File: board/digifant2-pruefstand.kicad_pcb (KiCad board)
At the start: 2 copper layers, 144 x 169 mm, 76 parts, among them J0 VW ECU HARNESS, J1 12V BENCH IN, J2 IDLE VALVE N71, J3 OLED / UI I2C, Q1 2N7002, Q2 P-MOS -30V >=5A, Q3 2N7002, Q5 2N7002, SW1 PUSH, SW2 PUSH, SW3 PUSH, U1 INA226 (0x40), U2 MCP4728 (0x60), U3 INA226 (0x41), U4 AD9833, U5 Raspberry Pi Pico, U6 TS5A3159A, U7 TS5A3159A, U8 TS5A3159A, Y1 25MHz

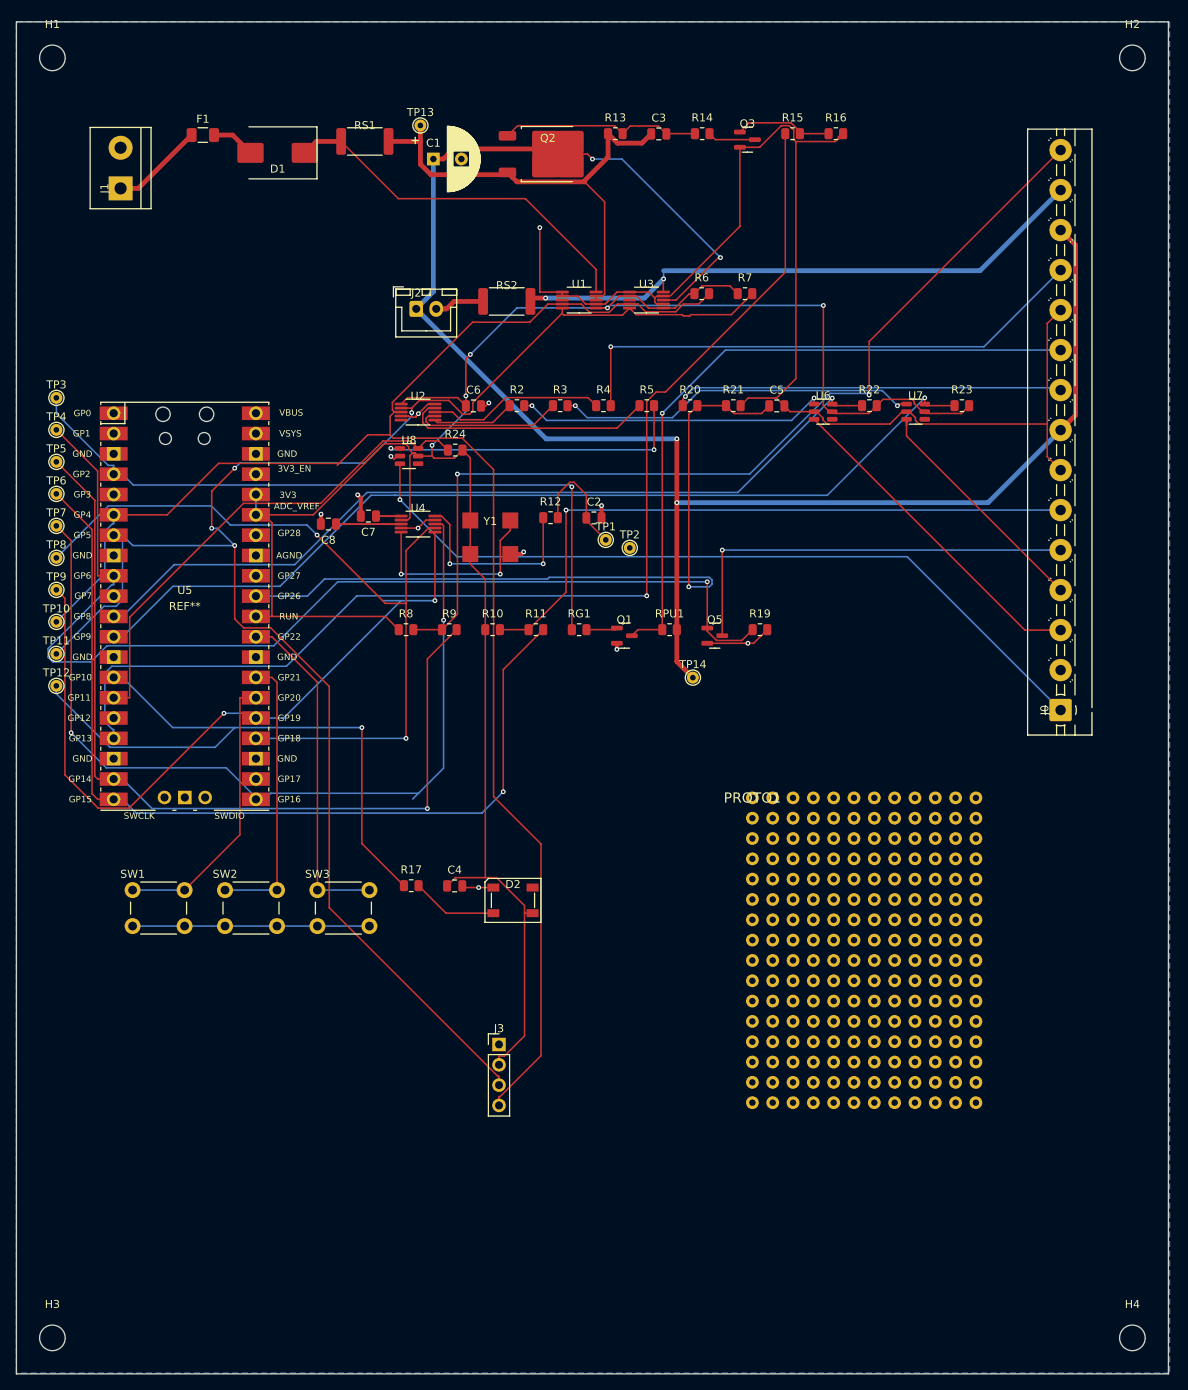
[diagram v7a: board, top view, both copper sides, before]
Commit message: Route remaining test points, add decoupling/thermal copper, trim board, label silkscreen
- Route TP7/TP8/TP9 (the three hardest, on U5's east side) with a purpose-built
  grid pathfinder after manual/Freerouting attempts kept snagging on the Pico's
  pin column, which has no usable gap anywhere along its length for a second
  trace; both had to detour around the south end of the module.
- Add C9/C10 (100nF) decoupling for U1/U3's VS pins per the INA226 datasheet,
  tapping the existing +3V3 trunk and GND pour near the packed U1/U3/RS1/RS2
  pocket.
- Add thermal copper pours for D1 (real risk: ~1.25W at sustained ~2.5A with
  no relief) and Q2, verified electrically connected via KiCad's connectivity
  API rather than just visually overlapping.
- Trim the board from 144x169mm to 144x150mm - the bottom 19mm was completely
  empty; move H3/H4 to keep the same edge margin as H1/H2.
- Add functional silkscreen labels next to J0 (real VW harness pin numbers)
  and every test point (moved from F.Fab, a documentation-only layer that
  never gets printed, to real F.SilkS; shortened long labels to fit the
  west-margin corridor without running off the board edge).
- Add fab-identification text (title/rev/date/company) to the previously
  empty back silkscreen, driven by the board's title block variables.
- Fix all 14 test points having "Exclude from BOM" set on the PCB side
  (schematic-parity check caught it) - they're real parts, not mechanical-only.
- Refill the GND zone after all of the above; confirmed the earlier
  "whole-board refill causes spurious violations" finding was a testing
  artifact (missing paired .kicad_pro), not a real issue.
- Regenerate the InteractiveHtmlBom output to include the newly-un-excluded
  test points.

Co-Authored-By: Claude Sonnet 5 <noreply@anthropic.com>
Claude-Session: https://claude.ai/code/session_01XcEuUwwCT37oProAm8HYeY
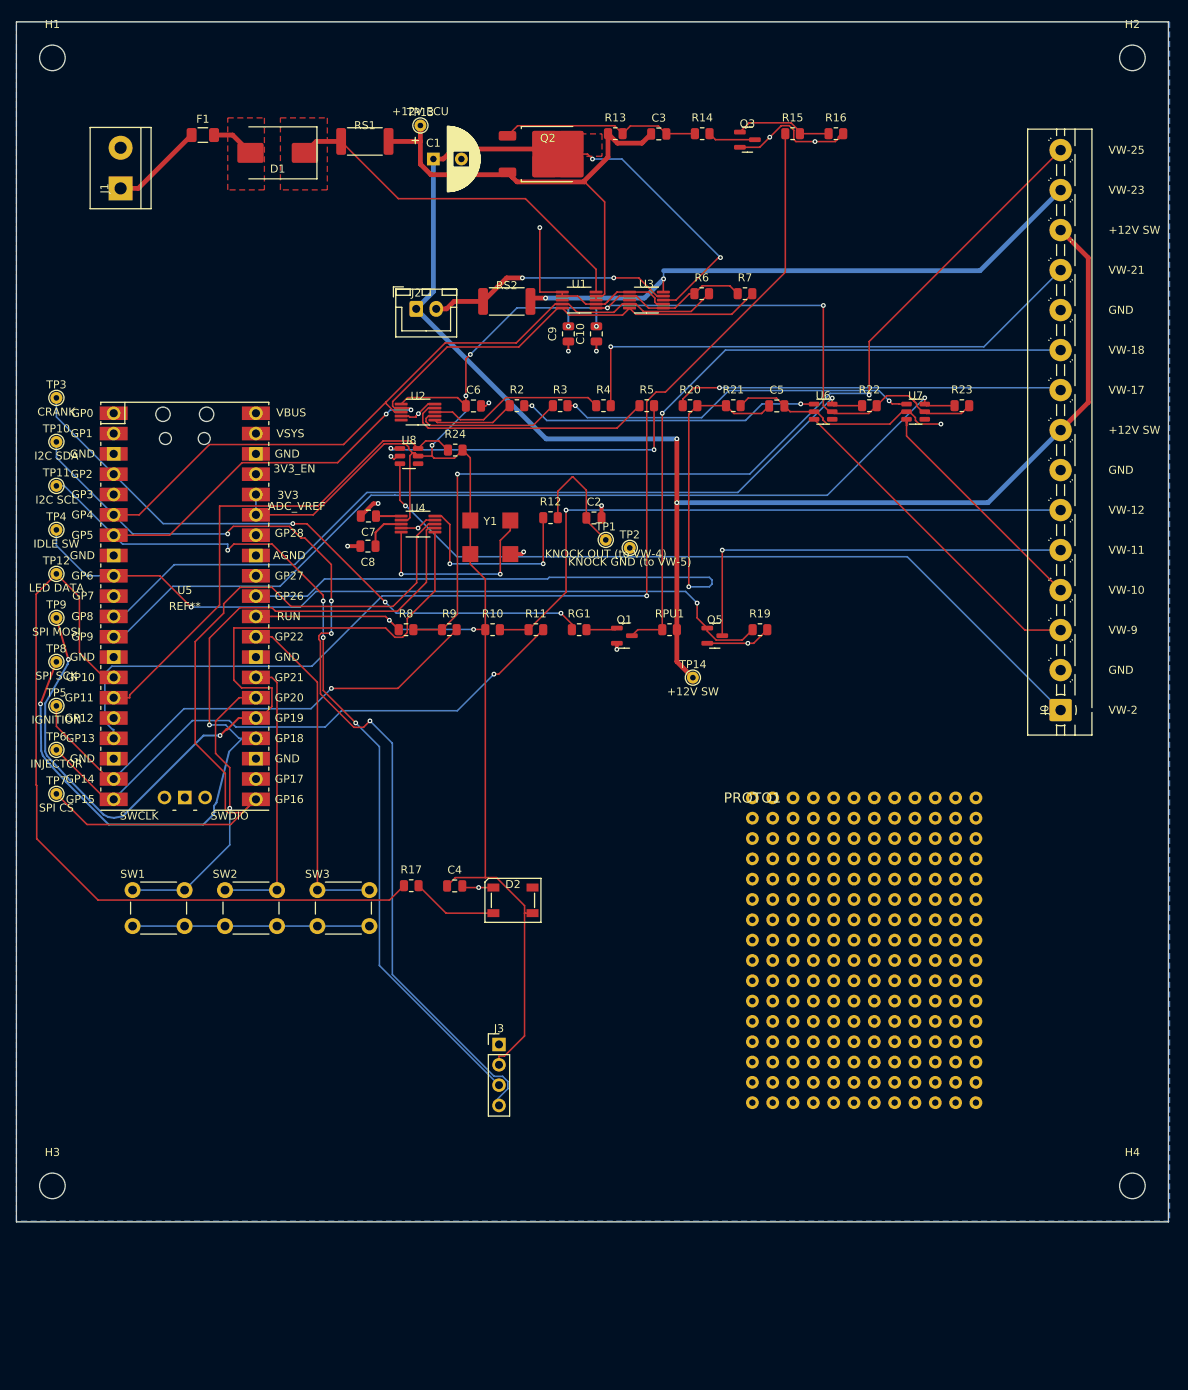
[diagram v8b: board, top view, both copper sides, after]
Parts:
- added C10: 100nF, Capacitor_SMD:C_0805_2012Metric, F.Cu at (72.5, 39.0)
- added C9: 100nF, Capacitor_SMD:C_0805_2012Metric, F.Cu at (69.0, 39.0)
- TP10: value TP I2C_SDA -> I2C SDA
- TP11: value TP I2C_SCL -> I2C SCL
- TP12: value TP GP10_LED_DATA -> LED DATA
- TP13: value TP +12V_ECU -> +12V ECU
- TP14: value TP +12V_ECU_SW -> +12V SW
- TP3: value TP GP2_CRANK -> CRANK
- TP4: value TP GP6_THROTTLE_IDLE_SW -> IDLE SW
- TP5: value TP GP14_IGN_CAPTURE -> IGNITION
- TP6: value TP GP15_INJ_CAPTURE -> INJECTOR
- TP7: value TP GP16_SPI_CS -> SPI CS
- TP8: value TP GP18_SPI_SCK -> SPI SCK
- TP9: value TP GP19_SPI_MOSI -> SPI MOSI
- moved TP7 33.5 mm to (5.00, 96.5)
- moved TP6 32.0 mm to (5.00, 91.0)
- moved TP5 30.5 mm to (5.00, 85.5)
- moved TP10 22.5 mm to (5.00, 52.5)
- moved TP11 21.0 mm to (5.00, 58.0)
- moved H3 19.0 mm to (4.50, 145.5)
- moved H4 19.0 mm to (139.5, 145.5)
- moved TP12 14.0 mm to (5.00, 69.0)
- moved TP8 13.0 mm to (5.00, 80.0)
- moved TP4 12.5 mm to (5.00, 63.5)
- moved C8 5.66 mm to (43.9, 65.5)
- moved TP9 3.50 mm to (5.00, 74.5)
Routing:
- net GND: track 223.5 -> 135.9 mm, vias 12 -> 17
- net GP14_IGN_CAPTURE: track 108.4 -> 63.0 mm
- net GP15_INJ_CAPTURE: track 115.2 -> 72.9 mm
- net GP6_THROTTLE_IDLE_SW: track 135.7 -> 97.4 mm, vias 1 -> 2
- net VALVE_RETURN_SENSE: track 7.54 -> 30.9 mm, vias 0 -> 2
- net GP10_LED_DATA: track 82.6 -> 100.6 mm, vias 1 -> 0
- net GP16_SPI_CS: track 111.0 -> 97.2 mm, vias 2 -> 0
- net GP19_SPI_MOSI: track 93.7 -> 105.7 mm
- net GP2_CRANK: track 88.7 -> 78.2 mm, vias 1 -> 3
- net I2C_SDA: track 206.5 -> 215.4 mm, vias 0 -> 4
- net GP18_SPI_SCK: track 98.5 -> 105.3 mm
- net +3V3: track 288.4 -> 292.8 mm, vias 5 -> 9
- net U4_CAP2V5: track 8.14 -> 5.35 mm
- net GP11_LAMBDA_CONNECT: track 62.2 -> 63.8 mm
- net GP20_BTN_MENU: track 35.4 -> 36.9 mm, vias 0 -> 1
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- added copper zone on F.Cu, net +12V_ECU_SW
- added copper zone on F.Cu, net +12V_POST_D1
- added copper zone on F.Cu, net +12V_PROT
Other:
- board size 144 x 169 mm -> 144 x 150 mm
- board text added: "${COMPANY}"
- board text added: "${TITLE}"
- board text added: "+12V SW"
- board text added: "GND"
- board text added: "REV ${REVISION} - ${ISSUE_DATE}"
- board text added: "VW-10"
- board text added: "VW-11"
- board text added: "VW-12"
- board text added: "VW-17"
- board text added: "VW-18"
- board text added: "VW-2"
- board text added: "VW-21"
- board text added: "VW-23"
- board text added: "VW-25"
- board text added: "VW-9"
